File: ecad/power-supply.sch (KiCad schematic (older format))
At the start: 0 parts

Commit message: Mostly complete schematic, about to tape out the PCB.
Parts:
- added C1, C3: 0.1u, Capacitors_SMD:C_0603_HandSoldering, symbol C
- added C10, C11, C12, C2, C4, C40, C41, C5: 22u, Capacitors_SMD:C_1210_HandSoldering, symbol C
- added C6: 10n, Capacitors_SMD:C_0603_HandSoldering, symbol C
- added C9: 39n, Capacitors_SMD:C_0603_HandSoldering, symbol C
- added D1: LED, LEDs:LED_0805_HandSoldering, symbol LED
- added J1: +15V, Pin_Headers:Pin_Header_Straight_2x02_Pitch2.54mm, symbol Conn_02x02_Counter_Clockwise
- added R1, R2, R3, R8, R9: 10k, Resistors_SMD:R_0603_HandSoldering, symbol R
- added R4: 82k, Resistors_SMD:R_0603_HandSoldering, symbol R
- added R7: 86k6, Resistors_SMD:R_0603_HandSoldering, symbol R
- added U1: ADR434BRZ, Housings_SOIC:SOIC-8_3.9x4.9mm_Pitch1.27mm, symbol ADR434BRZ
- added U10: NCV1117ST25T3G, TO_SOT_Packages_SMD:TO-252-2, symbol NCP1117-2.5_TO252
- added U2: OPA207IDR, Housings_SOIC:SOIC-8_3.9x4.9mm_Pitch1.27mm, symbol OPA207IDR
- added U3: ADP7104ARDZ-R7, feetprints:SOIC-8-EP, symbol ADP7104
- added U5: ADP7104ARDZ-5.0-R7, feetprints:SOIC-8-EP, symbol ADP7104
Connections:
- new net: R7.2, R8.1, R9.2, U3.2 (Adj)
- new net: D1.2 (A), R3.2, U3.7 (PG), U5.7 (PG)
- new net: C9.2, R9.1
- new net: R4.2, U1.7 (Comp)
- new net: C6.1, R4.1
- new net: C2.1, R1.2, R2.1, U2.3 (+)
- new net +12V: C1.1, C10.1, C3.2, C9.1, R1.1, R7.1, U1.2 (Vin), U2.7, U3.1 (Vout)
- new net +15V: C11.1, C4.1, C40.1, J1.1 (Pin_1), J1.2 (Pin_2), R3.1, U10.3 (VI), U3.5 (EN), U3.8 (Vin), U5.5 (EN), U5.8 (Vin)
- new net +2V5: C41.1, U10.2 (VO)
- new net +5V: C12.1, U5.1 (Vout), U5.2 (Adj)
- new net 4.096: C5.1, C6.2, U1.6 (Vout)
- new net BIAS: U2.2 (-), U2.6
- new net GND: C1.2, C10.2, C11.2, C12.2, C2.2, C3.1, C4.2, C40.2, C41.2, C5.2, D1.1 (K), J1.3 (Pin_3), J1.4 (Pin_4), R2.2, R8.2, U1.4 (GND), U10.1 (GND), U2.4, U3.3 (GND), U3.6 (GND), U3.9 (pad), U5.3 (GND), U5.6 (GND), U5.9 (pad)
- no-connect marks 0 -> 1
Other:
- note added: "4.096V ref"
- note added: "PG pulls low if power is not good.\n"
- note added: "Tab connects to Pin 2 (Out)\n"
- note added: "Vout = 1.22(1+r1/r2)\nr1 = (12/1.22 - 1) * r2\nr2 <= 200k"

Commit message: Rev A of board as ordered from Osh Park.
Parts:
- U3: value ADP7104ARDZ-R7 -> ADP7105ARDZ; symbol ADP7104 -> ADP7105
- U5: value ADP7104ARDZ-5.0-R7 -> ADP7104ARDZ-5.0; symbol ADP7104 -> ADP7105
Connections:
- no-connect marks 1 -> 3
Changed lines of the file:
@@
 $EndComp
 $Comp
-L ADP7104 U3
+L ADP7105 U3
 U 1 1 5A997D63
 P 3250 1700
 F 0 "U3" H 3200 2100 60  0000 C CNN
-F 1 "ADP7104ARDZ-R7" H 3200 2000 60  0000 C CNN
+F 1 "ADP7105ARDZ" H 3200 2000 60  0000 C CNN
 F 2 "feetprints:SOIC-8-EP" H 3200 1750 60  0001 C CNN
 F 3 "" H 3200 1750 60  0001 C CNN
@@
 $EndComp
 $Comp
-L ADP7104 U5
+L ADP7105 U5
 U 1 1 5A998ACD
 P 6500 1700
 F 0 "U5" H 6450 2100 60  0000 C CNN
-F 1 "ADP7104ARDZ-5.0-R7" H 6450 2000 60  0000 C CNN
+F 1 "ADP7104ARDZ-5.0" H 6450 2000 60  0000 C CNN
 F 2 "feetprints:SOIC-8-EP" H 6450 1750 60  0001 C CNN
 F 3 "" H 6450 1750 60  0001 C CNN
@@
 	3150 2050 3150 2150
 Wire Wire Line
-	3150 2150 3450 2150
-Wire Wire Line
-	3450 2150 3450 2050
-Wire Wire Line
-	3350 2050 3350 2150
-Connection ~ 3350 2150
-Wire Wire Line
-	3250 2150 3250 2200
+	3250 2050 3250 2200
 Connection ~ 3250 2150
 Wire Wire Line
@@
 	6400 2050 6400 2150
 Wire Wire Line
-	6400 2150 6700 2150
-Wire Wire Line
-	6700 2150 6700 2050
-Wire Wire Line
-	6600 2050 6600 2150
-Connection ~ 6600 2150
-Wire Wire Line
-	6500 2150 6500 2200
+	6500 2050 6500 2200
 Connection ~ 6500 2150
 Wire Wire Line
@@
 Text Notes 8400 2250 0    60   ~ 0
 Tab connects to Pin 2 (Out)\n
+Wire Wire Line
+	3150 2150 3350 2150
+Wire Wire Line
+	3350 2150 3350 2050
+NoConn ~ 3450 2050
+Wire Wire Line
+	6600 2150 6600 2050
+Wire Wire Line
+	6400 2150 6600 2150
+NoConn ~ 6700 2050
 $EndSCHEMATC

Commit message: Correct part name from adp7104 to adp7105, which has a soft start feature.
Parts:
- U5: value ADP7104ARDZ-5.0 -> ADP7105ARDZ-5.0
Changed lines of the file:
@@
 P 6500 1700
 F 0 "U5" H 6450 2100 60  0000 C CNN
-F 1 "ADP7104ARDZ-5.0" H 6450 2000 60  0000 C CNN
+F 1 "ADP7105ARDZ-5.0" H 6450 2000 60  0000 C CNN
 F 2 "feetprints:SOIC-8-EP" H 6450 1750 60  0001 C CNN
 F 3 "" H 6450 1750 60  0001 C CNN

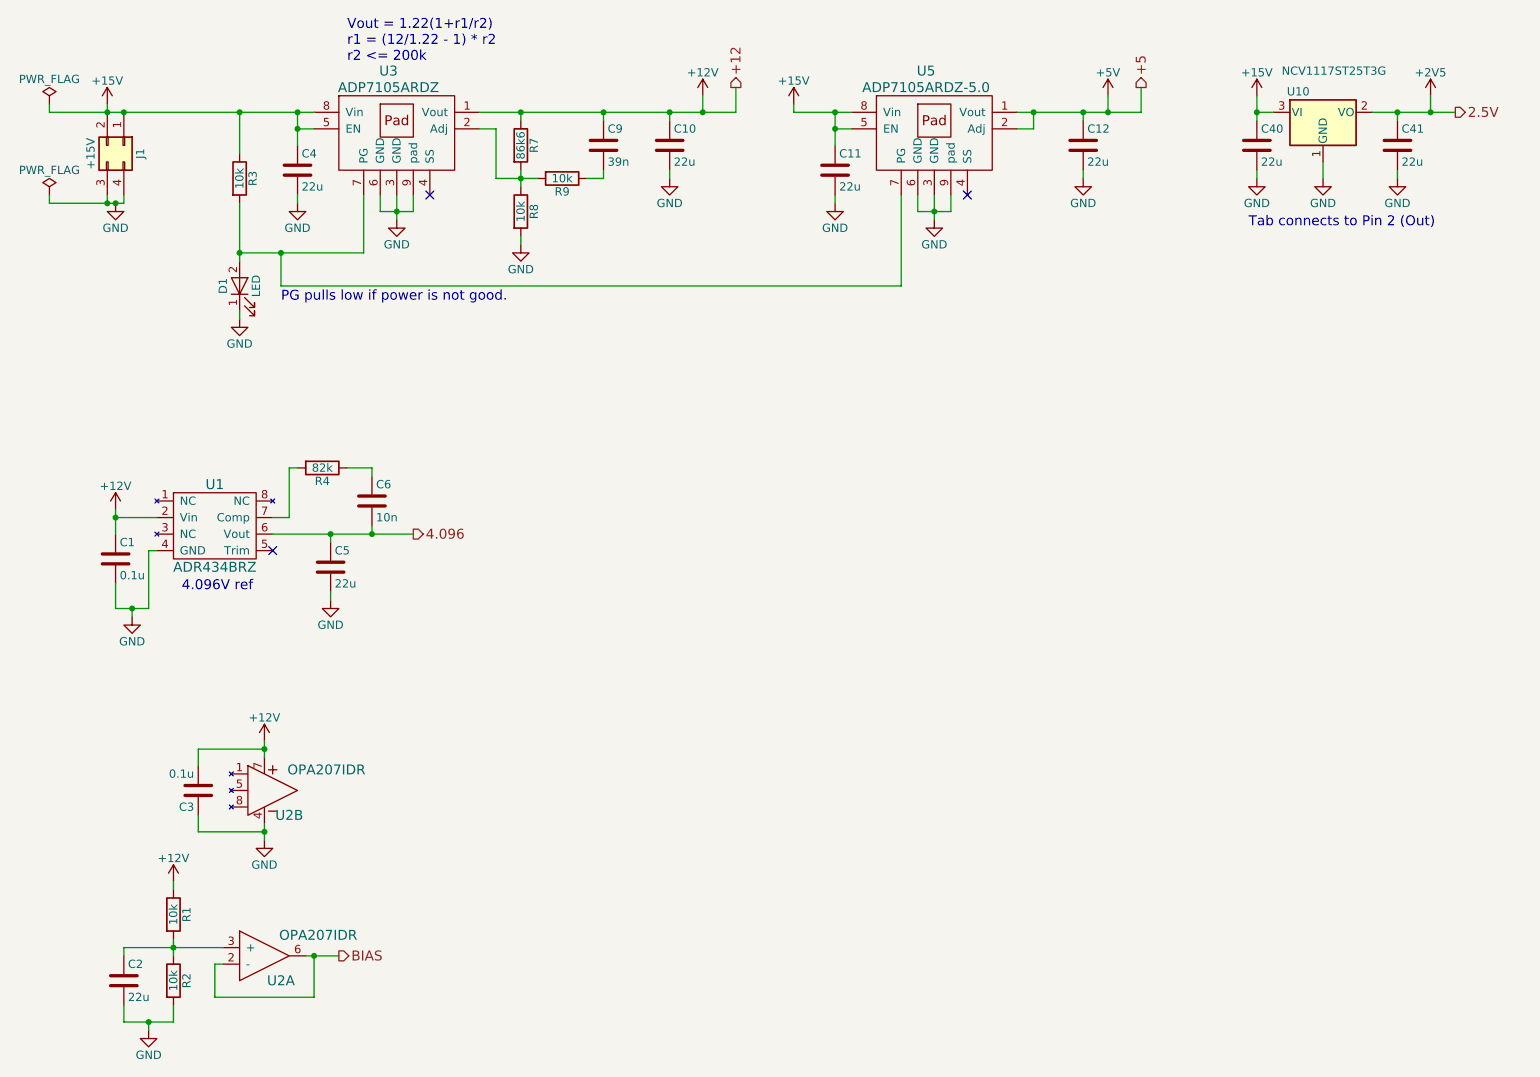
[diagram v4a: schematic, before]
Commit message: Slight changes to simulation and ecad with new changes before rollback to old changes.
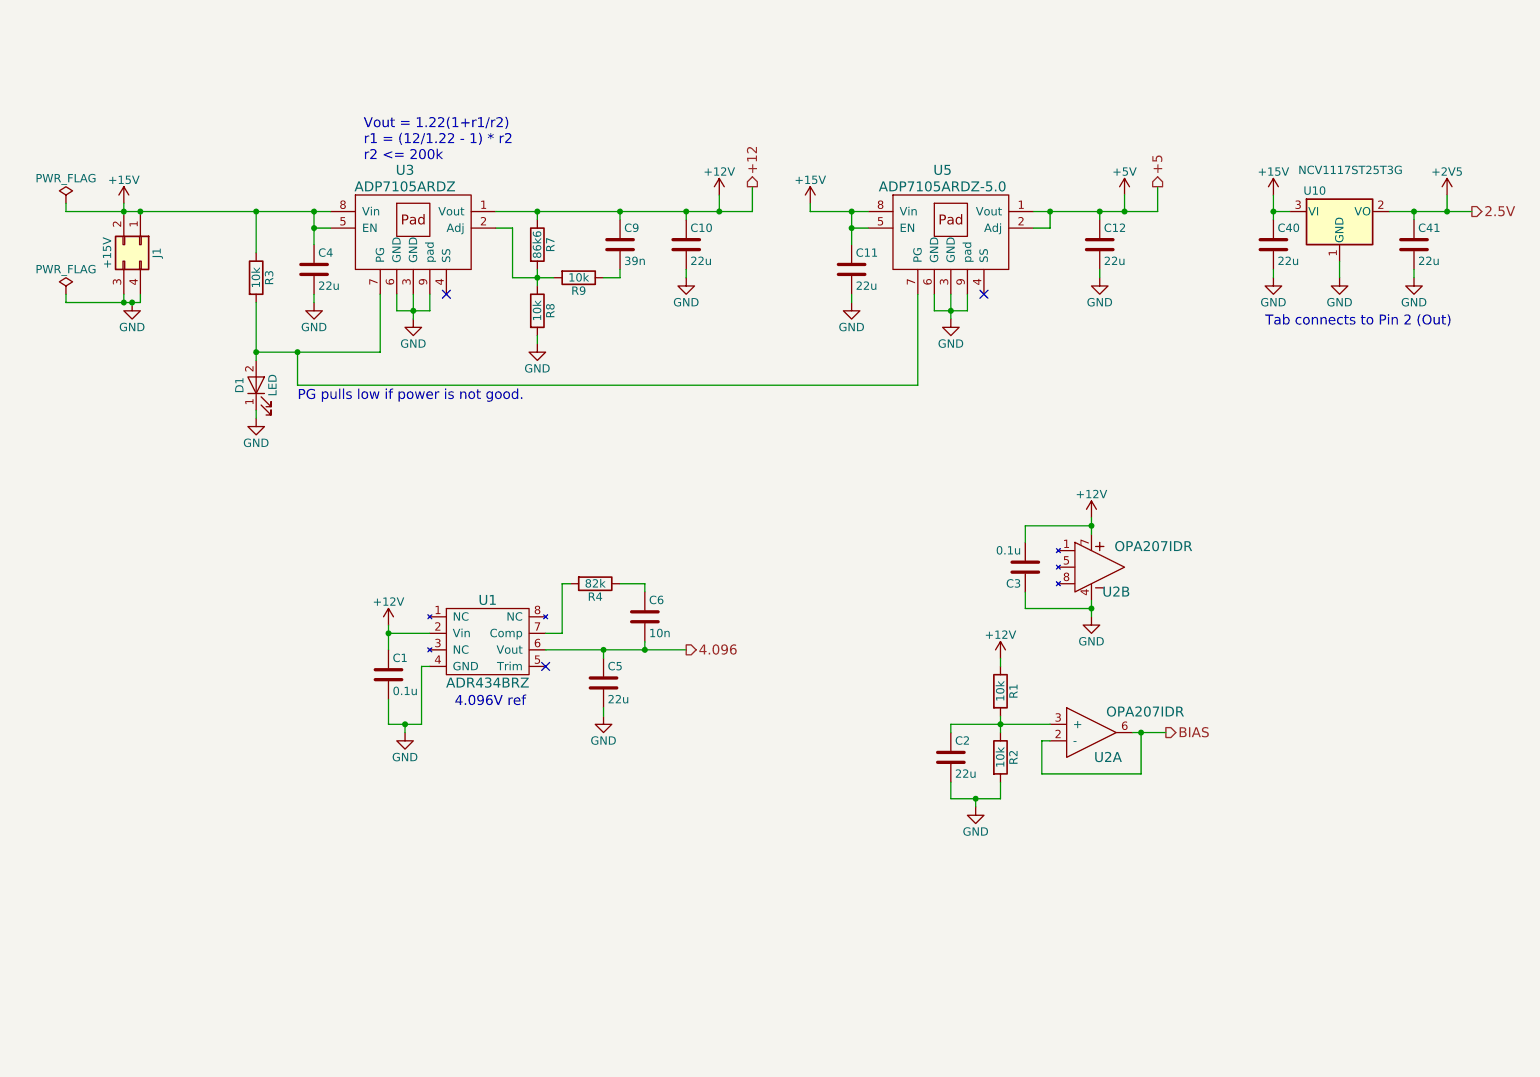
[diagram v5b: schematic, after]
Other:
- moved on the sheet: C1, C10, C11, C12, C2, C3, C4, C40, C41, C5, C6, C9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
